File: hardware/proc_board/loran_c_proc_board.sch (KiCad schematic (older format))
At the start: 33 parts, among them P101 Power, P102 Cortex SWD, P103 Clock board, U101 LD1117S33, U102 74AC14

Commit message: Update: fixed AGND zone on PCB
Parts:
- BT101: footprint (none) -> battery-hold:bh840
- FB102: footprint w_pth_resistors:RC07 -> w_pth_resistors:rc07_vert
- FB103: footprint w_pth_resistors:RC07 -> SMD_Packages:SM1812E
- MH101, MH102, MH103, MH104: footprint (none) -> holes:Hole_3-5mm
- P101: footprint (none) -> connect-minifit:minifit-8
- U101: footprint SMD_Packages:SOT223 -> Transistors_TO-220:TO-220_Neutral123_Vertical
- U102: footprint w_smd_dil:so-16 -> w_smd_dil:so-14
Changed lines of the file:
@@
 F 0 "U102" H 7950 3200 40  0000 C CNN
 F 1 "74AC14" H 8000 3000 40  0000 C CNN
-F 2 "w_smd_dil:so-16" H 7800 3100 60  0001 C CNN
+F 2 "w_smd_dil:so-14" H 7800 3100 60  0001 C CNN
 F 3 "" H 7800 3100 60  0000 C CNN
 	1    7800 3100
@@
 F 0 "U102" H 7950 5450 40  0000 C CNN
 F 1 "74AC14" H 8000 5250 40  0000 C CNN
-F 2 "w_smd_dil:so-16" H 7800 5350 60  0001 C CNN
+F 2 "w_smd_dil:so-14" H 7800 5350 60  0001 C CNN
 F 3 "" H 7800 5350 60  0000 C CNN
 	6    7800 5350
@@
 F 0 "U102" H 7950 3800 40  0000 C CNN
 F 1 "74AC14" H 8000 3600 40  0000 C CNN
-F 2 "w_smd_dil:so-16" H 7800 3700 60  0001 C CNN
+F 2 "w_smd_dil:so-14" H 7800 3700 60  0001 C CNN
 F 3 "" H 7800 3700 60  0000 C CNN
 	2    7800 3700
@@
 F 0 "U102" H 7950 4150 40  0000 C CNN
 F 1 "74AC14" H 8000 3950 40  0000 C CNN
-F 2 "w_smd_dil:so-16" H 7800 4050 60  0001 C CNN
+F 2 "w_smd_dil:so-14" H 7800 4050 60  0001 C CNN
 F 3 "" H 7800 4050 60  0000 C CNN
 	5    7800 4050
@@
 F 0 "U102" H 10500 3800 40  0000 C CNN
 F 1 "74AC14" H 10550 3600 40  0000 C CNN
-F 2 "w_smd_dil:so-16" H 10350 3700 60  0001 C CNN
+F 2 "w_smd_dil:so-14" H 10350 3700 60  0001 C CNN
 F 3 "" H 10350 3700 60  0000 C CNN
 	3    10350 3700
@@
 F 0 "U102" H 7950 4750 40  0000 C CNN
 F 1 "74AC14" H 8000 4550 40  0000 C CNN
-F 2 "w_smd_dil:so-16" H 7800 4650 60  0001 C CNN
+F 2 "w_smd_dil:so-14" H 7800 4650 60  0001 C CNN
 F 3 "" H 7800 4650 60  0000 C CNN
 	4    7800 4650
@@
 F 0 "FB102" H 10000 2900 60  0000 C CNN
 F 1 "Bead" H 10000 2650 60  0000 C CNN
-F 2 "w_pth_resistors:RC07" H 10000 2750 60  0001 C CNN
+F 2 "w_pth_resistors:rc07_vert" H 10000 2750 60  0001 C CNN
 F 3 "" H 10000 2750 60  0000 C CNN
 	1    10000 2750
@@
 F 0 "U101" H 8800 1450 40  0000 C CNN
 F 1 "LD1117S33" H 8800 1400 40  0000 C CNN
-F 2 "SMD_Packages:SOT223" H 8800 1200 60  0001 C CNN
+F 2 "Transistors_TO-220:TO-220_Neutral123_Vertical" H 8800 1200 60  0001 C CNN
 F 3 "" H 8800 1200 60  0000 C CNN
 	1    8800 1200
@@
 F 0 "BT101" H 1400 2950 50  0000 C CNN
 F 1 "Li CR2032" H 1400 2560 50  0000 C CNN
-F 2 "" H 1400 2750 60  0001 C CNN
+F 2 "battery-hold:bh840" H 1400 2750 60  0001 C CNN
 F 3 "" H 1400 2750 60  0000 C CNN
 	1    1400 2750
@@
 F 0 "FB103" H 7100 2400 60  0000 C CNN
 F 1 "Bead" H 7100 2150 60  0000 C CNN
-F 2 "w_pth_resistors:RC07" H 7100 2250 60  0001 C CNN
+F 2 "SMD_Packages:SM1812E" H 7100 2250 60  0001 C CNN
 F 3 "" H 7100 2250 60  0000 C CNN
 	1    7100 2250
@@
 F 0 "P101" V 5000 950 60  0000 C CNN
 F 1 "Power" V 5100 950 60  0000 C CNN
-F 2 "" H 5050 950 60  0000 C CNN
+F 2 "connect-minifit:minifit-8" H 5050 950 60  0001 C CNN
 F 3 "" H 5050 950 60  0000 C CNN
 	1    5050 950
@@
 F 0 "MH104" H 1800 2000 60  0000 C CNN
 F 1 "HOLE" H 1800 1620 60  0000 C CNN
-F 2 "" H 1800 1800 60  0000 C CNN
+F 2 "holes:Hole_3-5mm" H 1800 1800 60  0001 C CNN
 F 3 "" H 1800 1800 60  0000 C CNN
 	1    1800 1800
@@
 F 0 "MH103" H 1800 1450 60  0000 C CNN
 F 1 "HOLE" H 1800 1070 60  0000 C CNN
-F 2 "" H 1800 1250 60  0000 C CNN
+F 2 "holes:Hole_3-5mm" H 1800 1250 60  0001 C CNN
 F 3 "" H 1800 1250 60  0000 C CNN
 	1    1800 1250
@@
 F 0 "MH101" H 1000 1450 60  0000 C CNN
 F 1 "HOLE" H 1000 1070 60  0000 C CNN
-F 2 "" H 1000 1250 60  0000 C CNN
+F 2 "holes:Hole_3-5mm" H 1000 1250 60  0001 C CNN
 F 3 "" H 1000 1250 60  0000 C CNN
 	1    1000 1250
@@
 F 0 "MH102" H 1000 2000 60  0000 C CNN
 F 1 "HOLE" H 1000 1620 60  0000 C CNN
-F 2 "" H 1000 1800 60  0000 C CNN
+F 2 "holes:Hole_3-5mm" H 1000 1800 60  0001 C CNN
 F 3 "" H 1000 1800 60  0000 C CNN
 	1    1000 1800

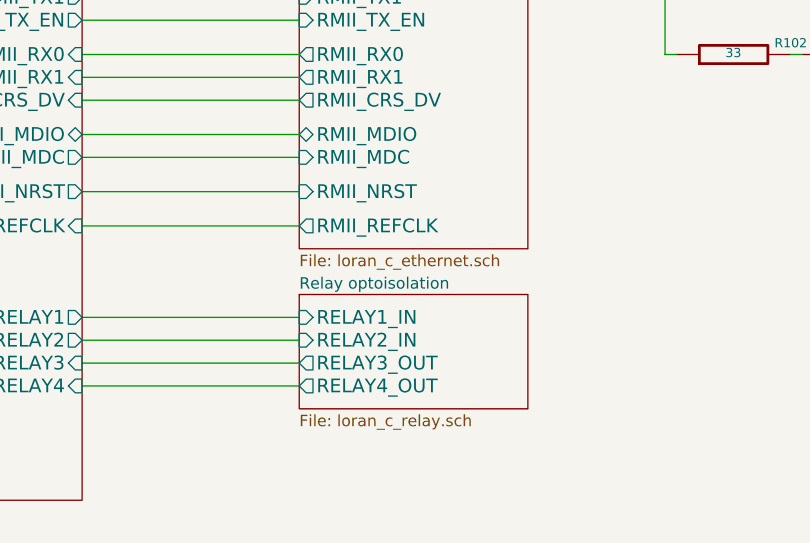
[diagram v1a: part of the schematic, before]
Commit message: PCB prototype production version, minor schematic updates PCB files sent to PCB house. PCB revision as of this commit can be treated as a first (and, hopefully, last) prototype version
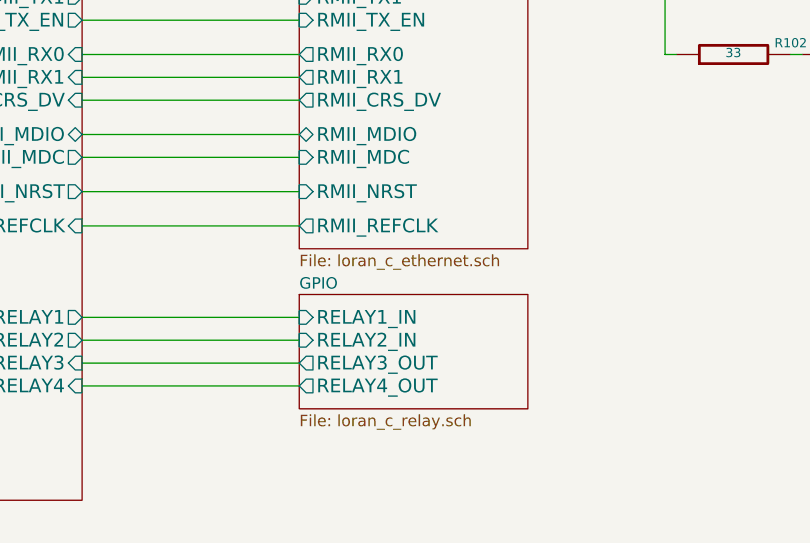
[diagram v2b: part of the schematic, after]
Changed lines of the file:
@@
 S 5150 6400 1000 500
 U 52DF2AF5
-F0 "Relay optoisolation" 50
+F0 "GPIO" 50
 F1 "loran_c_relay.sch" 50
 F2 "RELAY1_IN" I L 5150 6500 60

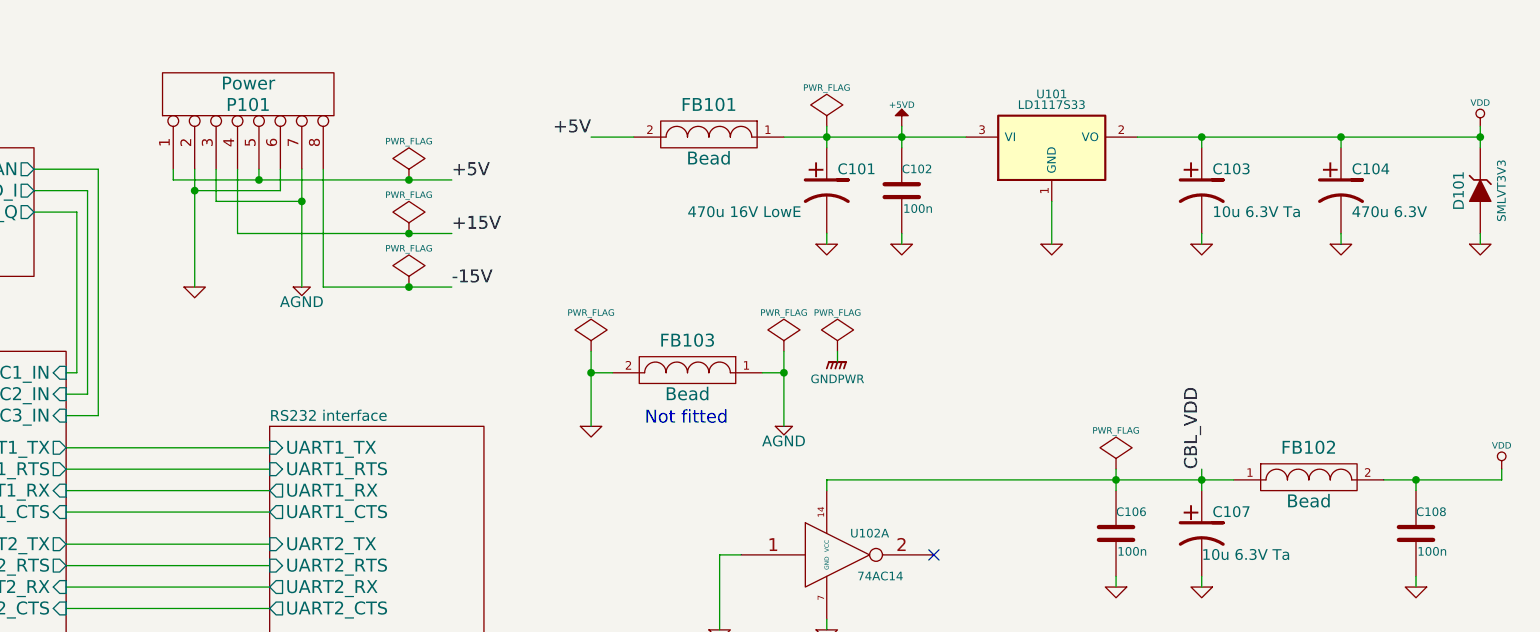
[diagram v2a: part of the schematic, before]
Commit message: Fix: nice MiniFit connector schematic symbol
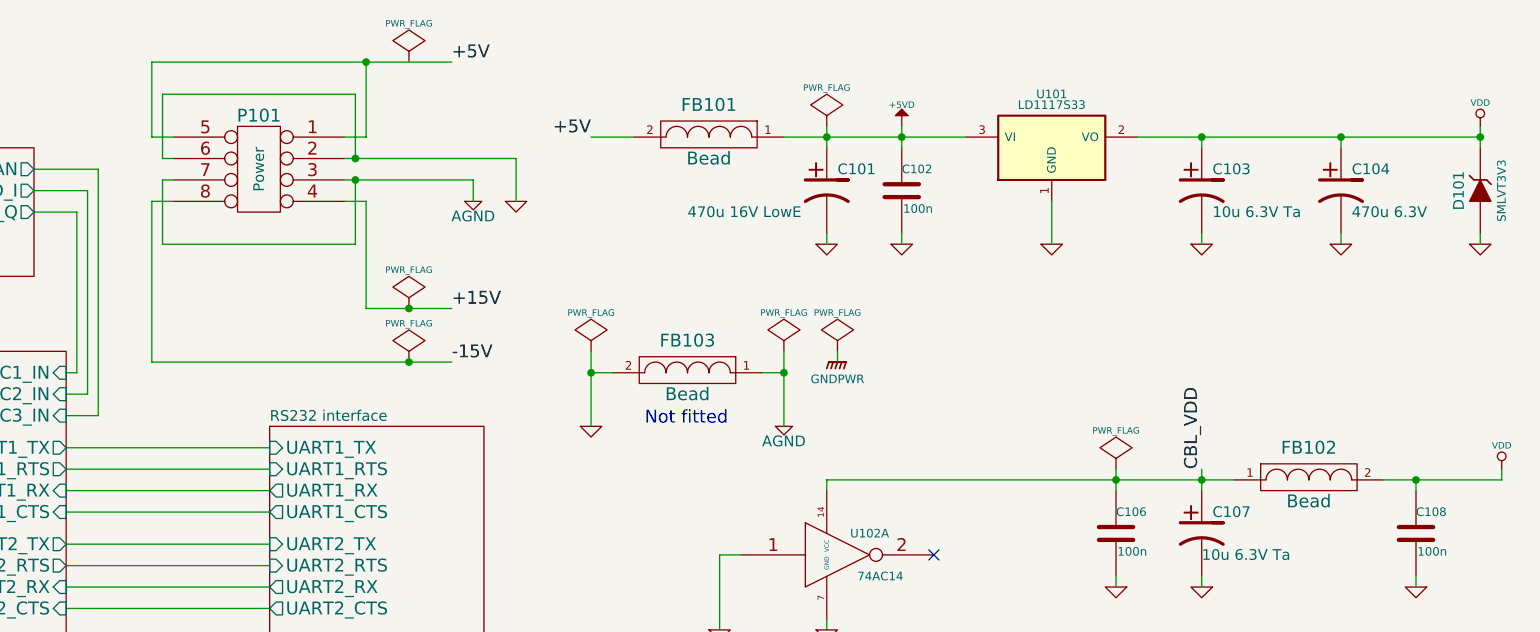
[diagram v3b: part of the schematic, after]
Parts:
- removed P101: Power, connect-minifit:minifit-8, symbol CONN_8
- added P101: Power, symbol MF_8
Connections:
- net +15V: now also P101.4
- net +5V: now also P101.1, P101.5
- net -15V: now also P101.8
- net AGND: now also P101.3, P101.7
- net GND: now also P101.2, P101.6
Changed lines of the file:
@@
 LIBS:crystal_shielded
 LIBS:conn_2s
+LIBS:conn_mf
 LIBS:loran_c_proc_board-cache
 EELAYER 24 0
@@
 L GND #PWR010
 U 1 1 52E67BFB
-P 4800 1850
-F 0 "#PWR010" H 4800 1850 30  0001 C CNN
-F 1 "GND" H 4800 1780 30  0001 C CNN
-F 2 "" H 4800 1850 60  0000 C CNN
-F 3 "" H 4800 1850 60  0000 C CNN
-	1    4800 1850
+P 6300 1450
+F 0 "#PWR010" H 6300 1450 30  0001 C CNN
+F 1 "GND" H 6300 1380 30  0001 C CNN
+F 2 "" H 6300 1450 60  0000 C CNN
+F 3 "" H 6300 1450 60  0000 C CNN
+	1    6300 1450
 	1    0    0    -1
 $EndComp
@@
 L AGND #PWR011
 U 1 1 52E69A33
-P 5300 1850
-F 0 "#PWR011" H 5300 1850 40  0001 C CNN
-F 1 "AGND" H 5300 1780 50  0000 C CNN
-F 2 "" H 5300 1850 60  0000 C CNN
-F 3 "" H 5300 1850 60  0000 C CNN
-	1    5300 1850
-	1    0    0    -1
-$EndComp
-Text Label 6000 1850 0    60   ~ 0
+P 6100 1450
+F 0 "#PWR011" H 6100 1450 40  0001 C CNN
+F 1 "AGND" H 6100 1380 50  0000 C CNN
+F 2 "" H 6100 1450 60  0000 C CNN
+F 3 "" H 6100 1450 60  0000 C CNN
+	1    6100 1450
+	1    0    0    -1
+$EndComp
+Text Label 6000 2200 0    60   ~ 0
 -15V
-Text Label 6000 1600 0    60   ~ 0
+Text Label 6000 1950 0    60   ~ 0
 +15V
 $Comp
 L PWR_FLAG #FLG012
 U 1 1 52E70920
-P 5800 1600
-F 0 "#FLG012" H 5800 1695 30  0001 C CNN
-F 1 "PWR_FLAG" H 5800 1780 30  0000 C CNN
-F 2 "" H 5800 1600 60  0000 C CNN
-F 3 "" H 5800 1600 60  0000 C CNN
-	1    5800 1600
+P 5800 1950
+F 0 "#FLG012" H 5800 2045 30  0001 C CNN
+F 1 "PWR_FLAG" H 5800 2130 30  0000 C CNN
+F 2 "" H 5800 1950 60  0000 C CNN
+F 3 "" H 5800 1950 60  0000 C CNN
+	1    5800 1950
 	1    0    0    -1
 $EndComp
@@
 L PWR_FLAG #FLG013
 U 1 1 52E709CE
-P 5800 1850
-F 0 "#FLG013" H 5800 1945 30  0001 C CNN
-F 1 "PWR_FLAG" H 5800 2030 30  0000 C CNN
-F 2 "" H 5800 1850 60  0000 C CNN
-F 3 "" H 5800 1850 60  0000 C CNN
-	1    5800 1850
+P 5800 2200
+F 0 "#FLG013" H 5800 2295 30  0001 C CNN
+F 1 "PWR_FLAG" H 5800 2380 30  0000 C CNN
+F 2 "" H 5800 2200 60  0000 C CNN
+F 3 "" H 5800 2200 60  0000 C CNN
+	1    5800 2200
 	1    0    0    -1
 $EndComp
@@
 	1    0    0    -1
 $EndComp
-Text Label 6000 1350 0    60   ~ 0
+Text Label 6000 800  0    60   ~ 0
 +5V
 $Comp
 L PWR_FLAG #FLG015
 U 1 1 52E75031
-P 5800 1350
-F 0 "#FLG015" H 5800 1445 30  0001 C CNN
-F 1 "PWR_FLAG" H 5800 1530 30  0000 C CNN
-F 2 "" H 5800 1350 60  0000 C CNN
-F 3 "" H 5800 1350 60  0000 C CNN
-	1    5800 1350
+P 5800 800
+F 0 "#FLG015" H 5800 895 30  0001 C CNN
+F 1 "PWR_FLAG" H 5800 980 30  0000 C CNN
+F 2 "" H 5800 800 60  0000 C CNN
+F 3 "" H 5800 800 60  0000 C CNN
+	1    5800 800
 	1    0    0    -1
 $EndComp
@@
 Not fitted
 $Comp
-L CONN_8 P101
-U 1 1 52E48614
-P 5050 950
-F 0 "P101" V 5000 950 60  0000 C CNN
-F 1 "Power" V 5100 950 60  0000 C CNN
-F 2 "connect-minifit:minifit-8" H 5050 950 60  0001 C CNN
-F 3 "" H 5050 950 60  0000 C CNN
-	1    5050 950
-	0    -1   -1   0
-$EndComp
-$Comp
 L HOLE MH104
 U 1 1 52EF52BD
@@
 Connection ~ 6650 2250
 Wire Wire Line
-	10900 2700 10900 2750
-Wire Wire Line
-	4700 1300 4700 1350
-Wire Wire Line
-	4700 1350 6000 1350
-Wire Wire Line
-	5100 1350 5100 1300
-Wire Wire Line
-	4800 1300 4800 1850
-Wire Wire Line
-	4800 1400 5200 1400
-Wire Wire Line
-	5200 1400 5200 1300
-Wire Wire Line
-	4900 1450 5300 1450
-Wire Wire Line
-	5300 1300 5300 1850
-Connection ~ 5100 1350
-Wire Wire Line
-	5000 1600 6000 1600
-Wire Wire Line
-	5400 1300 5400 1850
-Wire Wire Line
-	5400 1850 6000 1850
-Connection ~ 5800 1350
-Connection ~ 5800 1600
-Connection ~ 5800 1850
-Connection ~ 4800 1400
-Wire Wire Line
-	5000 1300 5000 1600
-Wire Wire Line
-	4900 1300 4900 1450
-Connection ~ 5300 1450
+	10900 2750 10900 2700
+Wire Wire Line
+	4600 2200 6000 2200
+Connection ~ 5800 1950
+Connection ~ 5800 2200
 Wire Wire Line
 	1600 1800 1400 1800
@@
 $EndComp
 Wire Wire Line
-	10900 2750 10350 2750
+	10350 2750 10900 2750
 Connection ~ 9100 5050
 Connection ~ 10000 5050
@@
 	1    0    0    -1
 $EndComp
+$Comp
+L MF_8 P101
+U 1 1 5317D8F2
+P 5100 1300
+F 0 "P101" H 5100 1550 60  0000 C CNN
+F 1 "Power" V 5100 1300 50  0000 C CNN
+F 2 "" H 5100 1100 60  0000 C CNN
+F 3 "" H 5100 1100 60  0000 C CNN
+	1    5100 1300
+	1    0    0    -1
+$EndComp
+Wire Wire Line
+	4600 800  6000 800
+Wire Wire Line
+	5600 800  5600 1150
+Wire Wire Line
+	5600 1150 5500 1150
+Wire Wire Line
+	4600 800  4600 1150
+Wire Wire Line
+	4600 1150 4700 1150
+Connection ~ 5600 800
+Wire Wire Line
+	5500 1450 5600 1450
+Wire Wire Line
+	5600 1450 5600 1950
+Wire Wire Line
+	5600 1950 6000 1950
+Wire Wire Line
+	4600 2200 4600 1450
+Wire Wire Line
+	4600 1450 4700 1450
+Wire Wire Line
+	5500 1250 6300 1250
+Wire Wire Line
+	6300 1250 6300 1450
+Wire Wire Line
+	6100 1350 6100 1450
+Wire Wire Line
+	5500 1350 6100 1350
+Wire Wire Line
+	4700 1350 4650 1350
+Wire Wire Line
+	4650 1350 4650 1650
+Wire Wire Line
+	4650 1650 5550 1650
+Wire Wire Line
+	5550 1650 5550 1350
+Connection ~ 5550 1350
+Wire Wire Line
+	4700 1250 4650 1250
+Wire Wire Line
+	4650 1250 4650 950
+Wire Wire Line
+	4650 950  5550 950
+Wire Wire Line
+	5550 950  5550 1250
+Connection ~ 5550 1250
 $EndSCHEMATC
